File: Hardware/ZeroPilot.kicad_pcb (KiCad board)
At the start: 2 copper layers, 100 x 100 mm, 197 parts, among them J1 CONN_01X04, J10 PWM, J11 PWM, J12 PWM, J13 PWM, J14 SPOX-2, J15 CONN_02X05, J16 SPOX-3, J17 SPOX-3, J18 SPOX-4, J19 SPOX-2, J2 PWM, J20 SPOX-3, J21 SPOX-3, J22 SPOX-3, J23 SPOX-5, J24 SPOX-5, J25 SPOX-4, J26 SPOX-4, J27 SPOX-4, J28 SPOX-6, J29 SPOX-6, J3 PWM, J30 SPOX-6, J31 SPOX-6, J32 CONN_01X02, J33 SPOX-6, J34 SPOX-6, J35 SPOX-6, J36 SPOX-6, J37 Micro_SD_Card, J4 PWM, J5 PWM, J6 PWM, J7 PWM, J8 PWM, J9 PWM, Q1 Q_PMOS_DGS, U1 NLAS4599, U10 NLAS4599, U11 NLAS4599, U12 NLAS4599, U13 TS30013-M050QFNR, U14 TS30013-M050QFNR, U15 MCP1826S-3302E/DB, U16 STM32F765ZGT6, U17 NC7SZ125P5X, U18 NC7SZ125P5X, U19 STM32F030R8T6, U2 NLAS4599, U20 M24C64-WDW6TP, U3 NLAS4599, U4 NLAS4599, U5 NLAS4599, U6 NLAS4599, U7 NLAS4599, U8 NLAS4599, U9 NLAS4599, Y1 32.768kHz, Y2 8MHz

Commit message: realizing how hard routing headers is
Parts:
- moved TP2 80.1 mm to (79.9, 113.6)
- moved R34 73.2 mm to (91.7, 143.3)
- moved R31 66.1 mm to (95.8, 143.3), turned to 180 degrees
- moved R33 21.1 mm to (144.6, 120.4)
- moved R32 14.3 mm to (147.2, 115.8)
- moved R35 5.37 mm to (146.1, 111.5)
- moved R30 4.38 mm to (146.6, 112.7)
- moved C11 0.88 mm to (104.8, 108.8), turned to 135 degrees
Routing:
- net /MOSI5: track 0.00 -> 56.0 mm, vias 0 -> 2
- net /SCK5: track 0.00 -> 55.5 mm, vias 0 -> 2
- net /SDA2: track 0.00 -> 50.6 mm
- net /SCL2: track 0.00 -> 49.8 mm
- net /MISO5: track 0.00 -> 48.4 mm, vias 0 -> 2
- net /NSS5: track 0.00 -> 35.1 mm
- net /SCK4: track 0.00 -> 29.4 mm
- net /MOSI4: track 0.00 -> 27.5 mm
- net /SCLK_PILOT: track 53.8 -> 26.8 mm, vias 4 -> 3
- net /MISO4: track 0.00 -> 24.3 mm
- net /NSS4: track 0.00 -> 21.4 mm
- net /NSS2: track 0.00 -> 17.2 mm
- net /SCK2: track 0.00 -> 16.9 mm
- net /RTS4: track 0.00 -> 16.1 mm
- net /CTS4: track 0.00 -> 15.1 mm
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
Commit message: finished signal routing
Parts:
- moved R30 73.8 mm to (79.4, 143.3)
- moved R33 70.3 mm to (77.4, 141.2), turned to 180 degrees
- moved R35 56.2 mm to (99.8, 143.3)
- moved R32 51.3 mm to (103.8, 143.2)
- moved TP1 5.57 mm to (86.4, 118.5)
- moved TP39 3.99 mm to (90.9, 114.2)
- moved J19 1.61 mm to (122.1, 103.6)
- moved J17 0.82 mm to (123.1, 96.0)
- moved D19 0.52 mm to (111.5, 86.9)
- moved R53 0.33 mm to (122.5, 100.0)
- moved C20 0.28 mm to (101.8, 85.2)
- moved C13 0.20 mm to (111.8, 95.5)
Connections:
- R33 pad 2: /SCL1 -> /SDA1
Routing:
- net /3V3: track 44.1 -> 179.7 mm, vias 0 -> 6
- net /5V_INT: track 116.0 -> 224.5 mm, vias 12 -> 13
- net /SDA4: track 22.9 -> 116.8 mm, vias 0 -> 2
- net /SCL4: track 24.0 -> 115.3 mm, vias 2 -> 5
- net /5V_EXT: track 49.5 -> 137.1 mm
- net /CTS7: track 0.00 -> 83.9 mm, vias 0 -> 2
- net /ULTRA_SONIC_1: track 0.00 -> 82.0 mm, vias 0 -> 2
- net /ULTRA_SONIC_2: track 0.00 -> 81.4 mm, vias 0 -> 2
- net /TX7: track 0.00 -> 78.5 mm, vias 0 -> 4
- net /RTS7: track 0.00 -> 76.6 mm, vias 0 -> 2
- net /RX4: track 0.00 -> 74.2 mm, vias 0 -> 2
- net /TX4: track 0.00 -> 73.9 mm, vias 0 -> 2
- net /RX7: track 57.0 -> 125.9 mm, vias 4 -> 6
- net /CTS1: track 0.03 -> 62.7 mm, vias 0 -> 2
- net /RX1: track 0.02 -> 61.2 mm, vias 0 -> 2
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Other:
- outline, holes or cut-outs redrawn

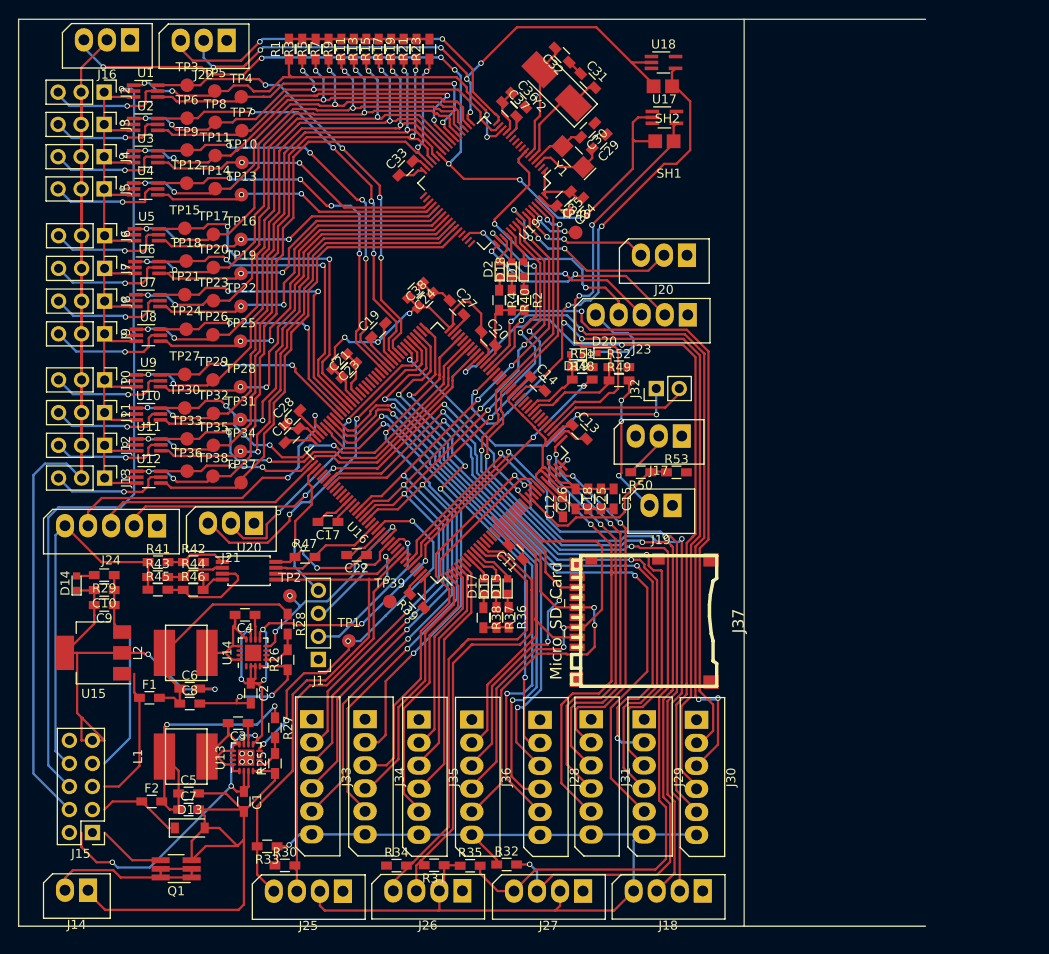
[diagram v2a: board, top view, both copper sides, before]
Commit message: finished all routing except gnd
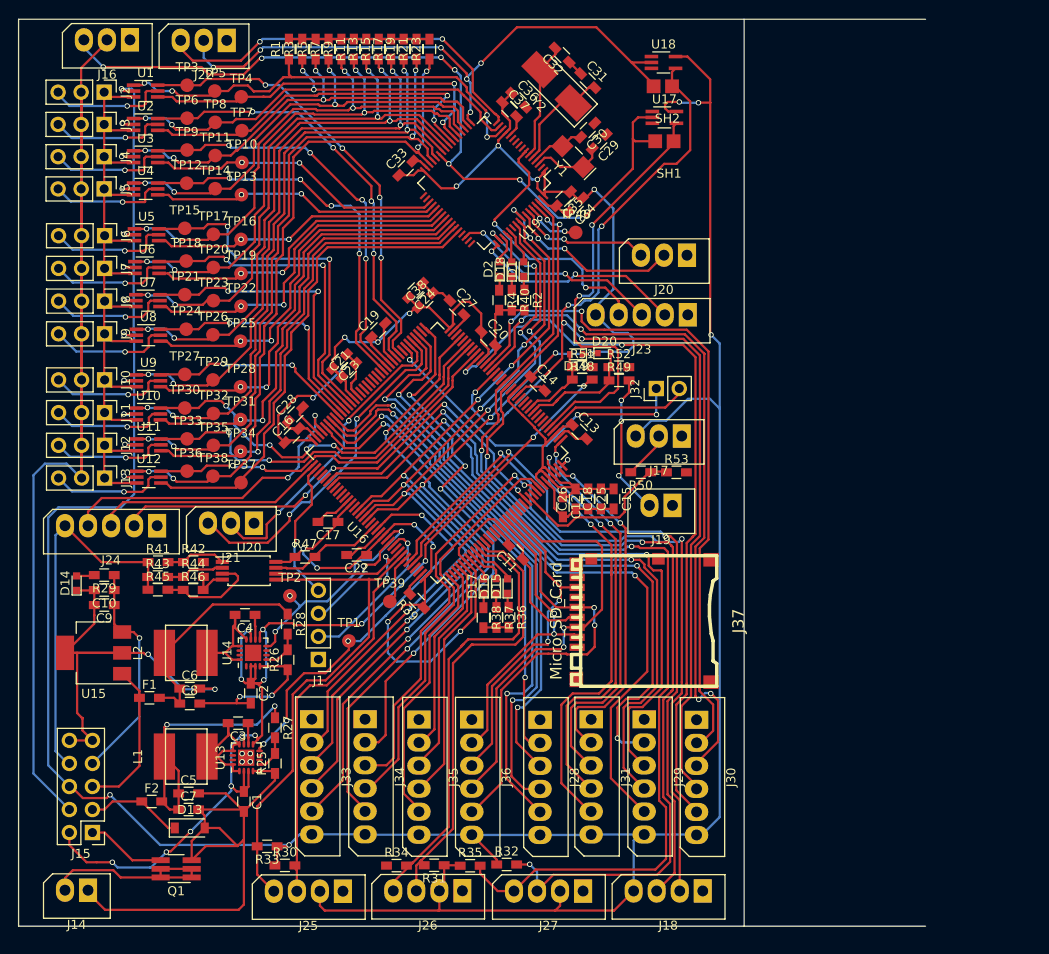
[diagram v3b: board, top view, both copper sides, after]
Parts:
- moved C28 0.45 mm to (80.5, 93.6)
- turned C12 to 270 degrees
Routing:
- net /5V_INT: track 224.5 -> 360.3 mm, vias 13 -> 17
- net /3V3: track 179.7 -> 299.2 mm, vias 6 -> 17
- net /POWER/3V3_JMP: track 7.02 -> 25.2 mm, vias 0 -> 1
- net (no net): track 16.2 -> 0.00 mm
- net Net-(TP39-Pad1): track 0.02 -> 5.52 mm
- net GND: track 302.9 -> 308.1 mm
- net /PW_GOOD_EXT: track 40.8 -> 44.2 mm
- net /NSS2: track 58.1 -> 61.2 mm
- net /MISO1: track 81.7 -> 84.6 mm
- net /SCK2: track 64.7 -> 67.6 mm
- net /SCK1: track 87.7 -> 90.4 mm
- net /NSS1: track 80.5 -> 83.2 mm
- net /MOSI1: track 88.3 -> 91.0 mm
- net /POWER/5V_INT_JMP: track 15.2 -> 17.1 mm
- net /VBATT: track 117.0 -> 118.5 mm, vias 12 -> 14
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
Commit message: A fully routed (shitty) board!
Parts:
- moved R50 0.06 mm to (118.7, 99.9)
- moved R53 0.05 mm to (122.6, 99.9)
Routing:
- net GND: track 308.1 -> 427.1 mm, vias 8 -> 69
- net /3V3: track 299.2 -> 315.5 mm, vias 17 -> 19
- net /5V_INT: track 360.3 -> 364.7 mm
- net /PILOT CONTROLLER/ADC3_IN10: track 20.1 -> 20.7 mm
- net Net-(D16-Pad2): track 4.23 -> 3.71 mm
- net /PILOT CONTROLLER/JRST: vias 1 -> 2
- added copper zone on B.Cu, net GND
- added copper zone on F.Cu, net GND

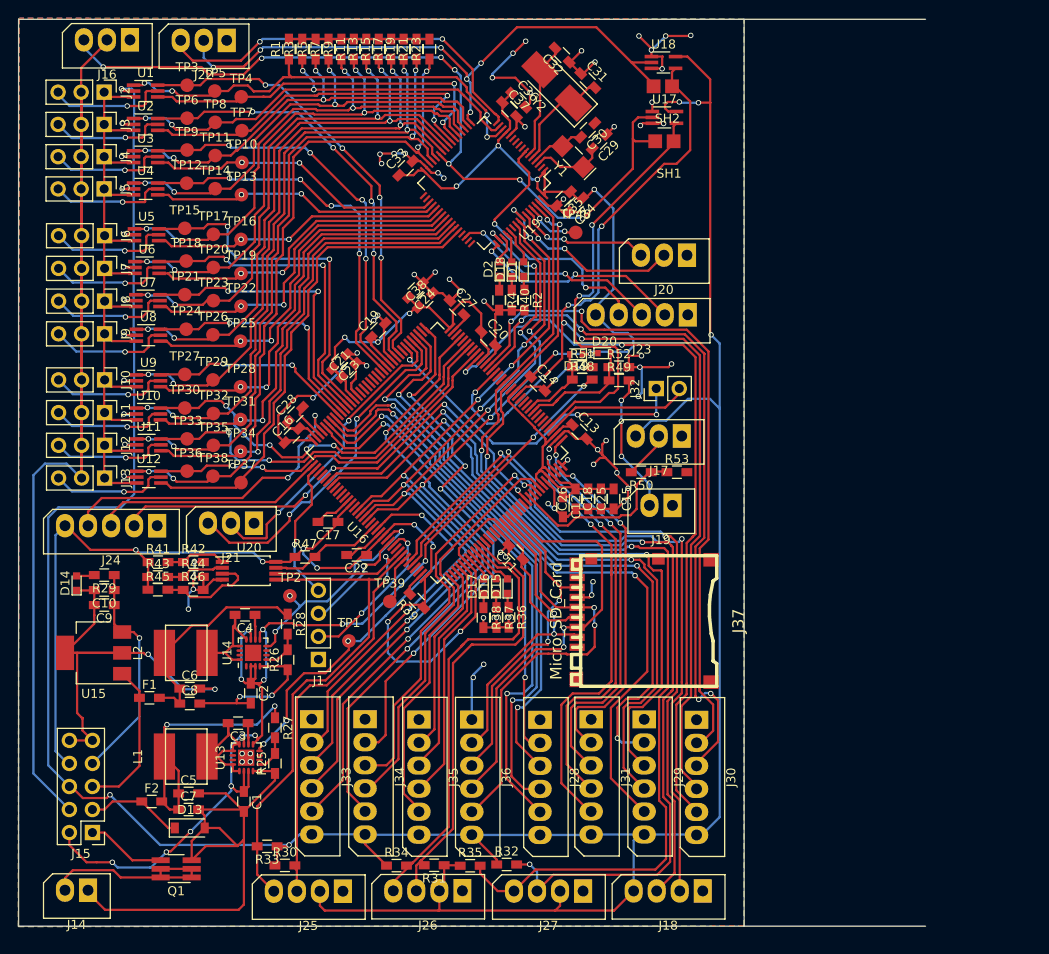
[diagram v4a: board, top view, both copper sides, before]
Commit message: Fixed random connection errors
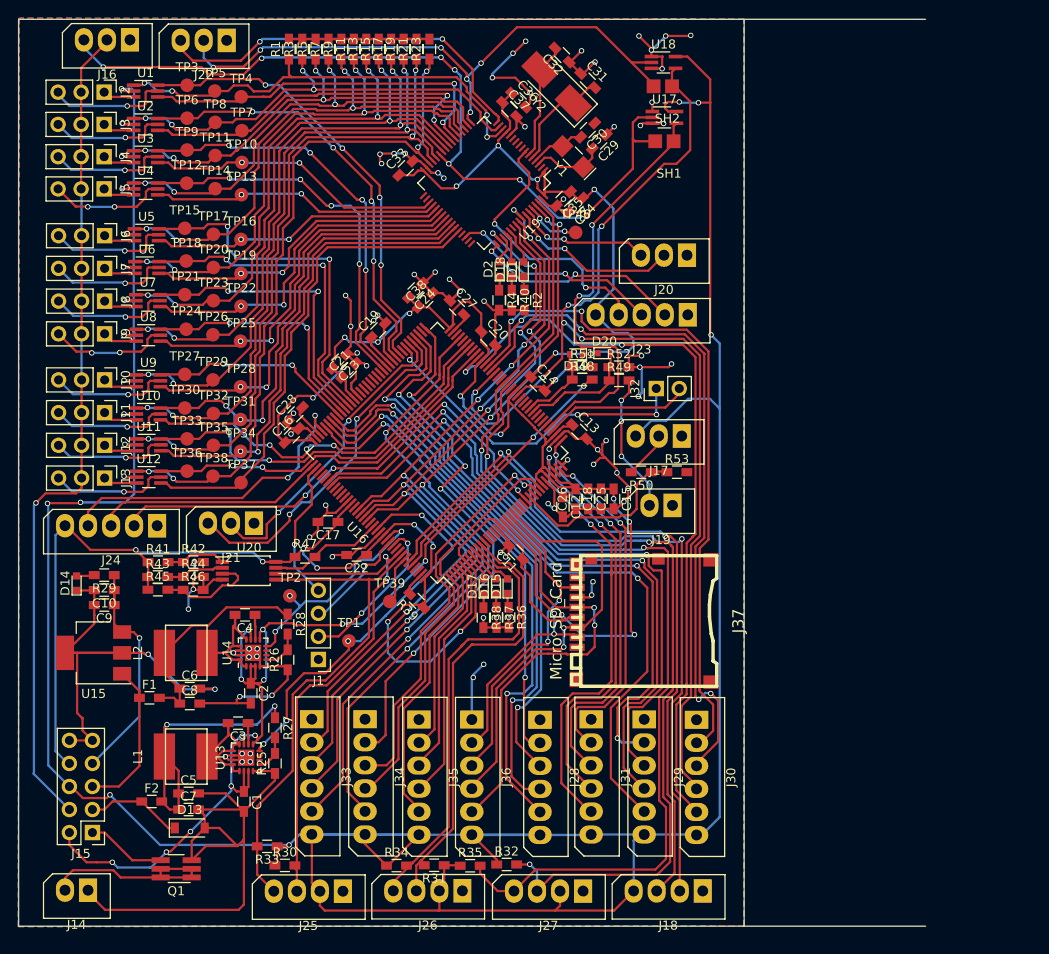
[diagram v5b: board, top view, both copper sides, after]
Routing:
- net /5V_EXT: track 137.1 -> 92.1 mm, vias 0 -> 1
- net /3V3: track 315.5 -> 357.9 mm, vias 19 -> 25
- net /5V_INT: track 364.7 -> 396.7 mm, vias 17 -> 19
- net GND: track 427.1 -> 407.8 mm, vias 69 -> 82
- net /POWER/3V3_JMP: track 25.2 -> 26.8 mm
- net Net-(C4-Pad2): track 12.7 -> 13.8 mm
- net Net-(J5-Pad3): track 12.7 -> 13.1 mm, vias 1 -> 2
- net Net-(J9-Pad3): track 13.4 -> 13.3 mm, vias 1 -> 2

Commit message: This power is HUGE
Made some big traces and pours for power. Need to do some ground layer
stiching to fix the ground plane still
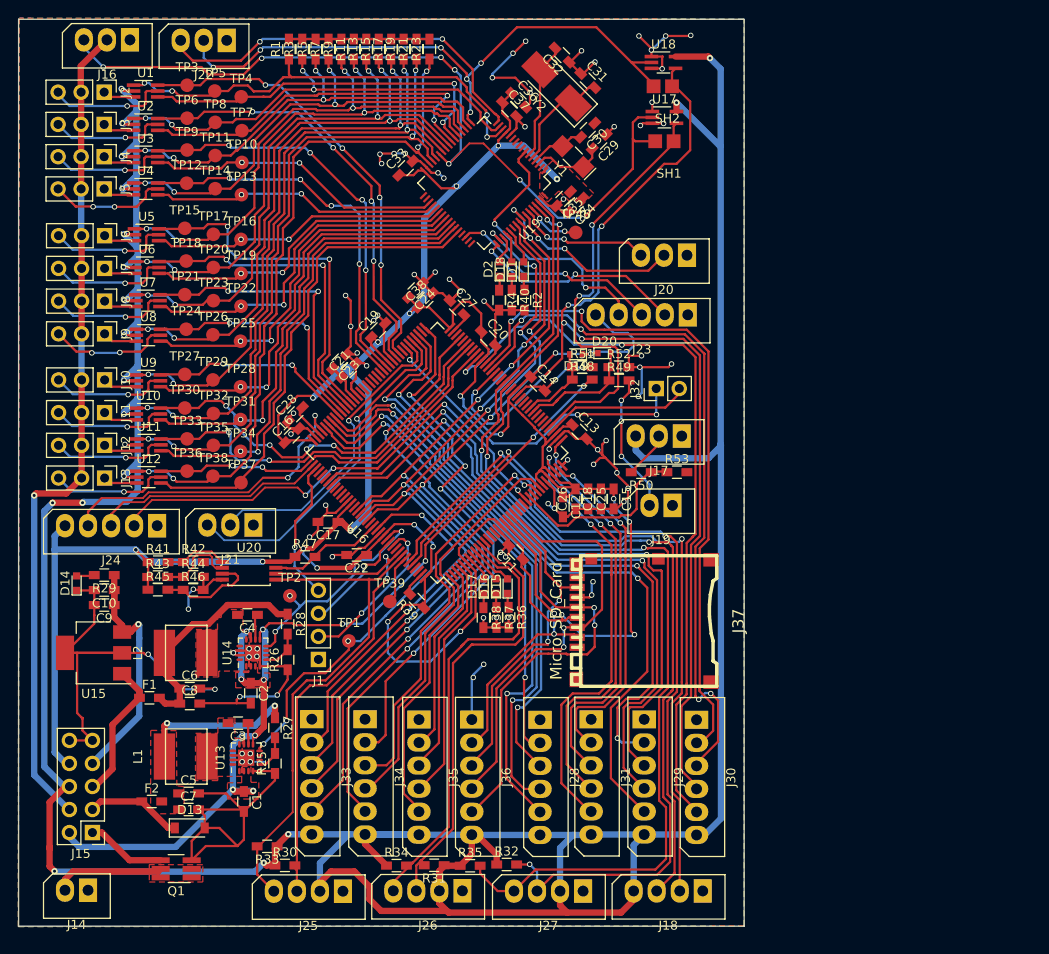
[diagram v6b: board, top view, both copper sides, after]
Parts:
- moved C4 0.27 mm to (75.2, 115.7)
- moved J21 0.21 mm to (75.9, 105.8)
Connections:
- net Net-(C3-Pad2) renamed /POWER/5V_EXT_OUT
- net Net-(C4-Pad2) renamed /POWER/5V_INT_OUT
- net Net-(C5-Pad1) renamed /POWER/5V_EXT_PREFUSE
- net Net-(C6-Pad1) renamed /POWER/5V_INT_PREFUSE
- net Net-(J14-Pad2) renamed /POWER/BATT_IN
- net Net-(R25-Pad2) renamed /POWER/5V_EXT_FB
- net Net-(R26-Pad2) renamed /POWER/5V_INT_FB
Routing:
- net GND: track 407.8 -> 384.0 mm, vias 82 -> 79
- net /5V_INT: track 396.7 -> 418.8 mm
- net /3V3: track 357.9 -> 374.3 mm, vias 25 -> 24
- net /POWER/5V_INT_OUT: track 13.8 -> 0.05 mm
- net /POWER/5V_EXT_OUT: track 16.5 -> 3.38 mm
- net /POWER/5V_EXT_PREFUSE: track 31.5 -> 18.4 mm
- net /VBATT: track 118.5 -> 109.2 mm, vias 14 -> 12
- net /POWER/BATT_IN: track 21.3 -> 12.2 mm
- net /MEMORY/E2: track 6.45 -> 8.67 mm
- net /PPM: track 93.2 -> 95.2 mm
- net /POWER/3V3_JMP: track 26.8 -> 28.5 mm
- net /SCLK_PILOT: track 55.0 -> 56.6 mm
- net /POWER/5V_INT_JMP: track 17.1 -> 15.9 mm
- net /POWER/5V_INT_PREFUSE: track 24.9 -> 25.8 mm
- net /RX3: track 34.1 -> 34.9 mm, vias 2 -> 1
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- added copper zone on F.Cu, net /3V3
- added copper zone on F.Cu, net /POWER/5V_EXT_OUT
- added copper zone on F.Cu, net /POWER/5V_EXT_PREFUSE
- added copper zone on F.Cu, net /POWER/5V_INT_OUT
- added copper zone on F.Cu, net /POWER/BATT_IN
- added copper zone on F.Cu, net /VBATT
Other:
- board size 100 x 100 mm -> 80 x 100 mm
- net class Default: clearance 0.2 -> 0.19999; trace_width 0.25 -> 0.2032; via_dia 0.6 -> 0.6858; via_drill 0.4 -> 0.3302
- net class PWR added: clearance 0.19999, trace_width 0.7, via_dia 0.6858, via_drill 0.3302
- rule trace_clearance: 0.2 -> 0.19999
- rule trace_min: 0.2 -> 0.2032
- rule via_min_size: 0.4 -> 0.6
